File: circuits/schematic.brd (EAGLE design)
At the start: 87.9 x 43.8 mm, 42 parts, among them IC1 MEGA8-P, IC2 MAX481CPA, J1 AVR_SPI_PRG_6PTH

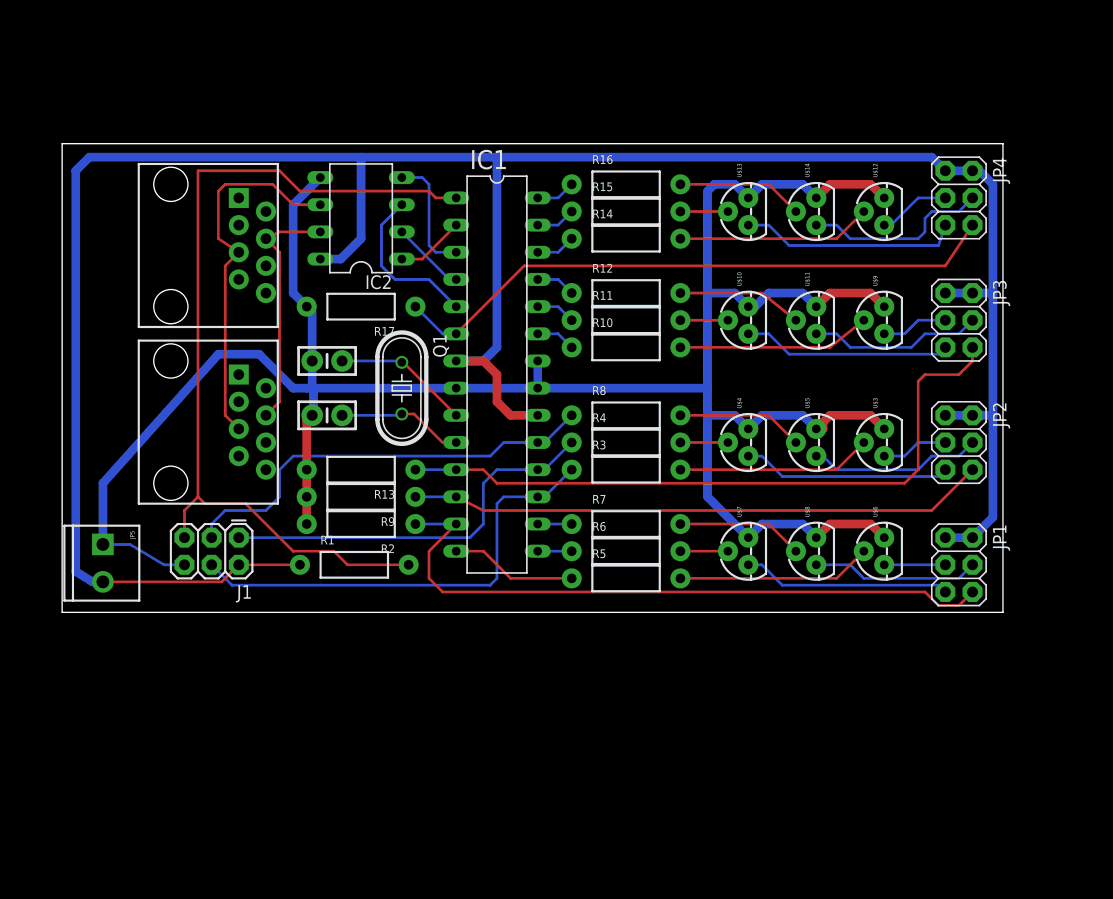
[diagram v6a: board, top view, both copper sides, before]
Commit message: Fix RJ45 jack footprint.
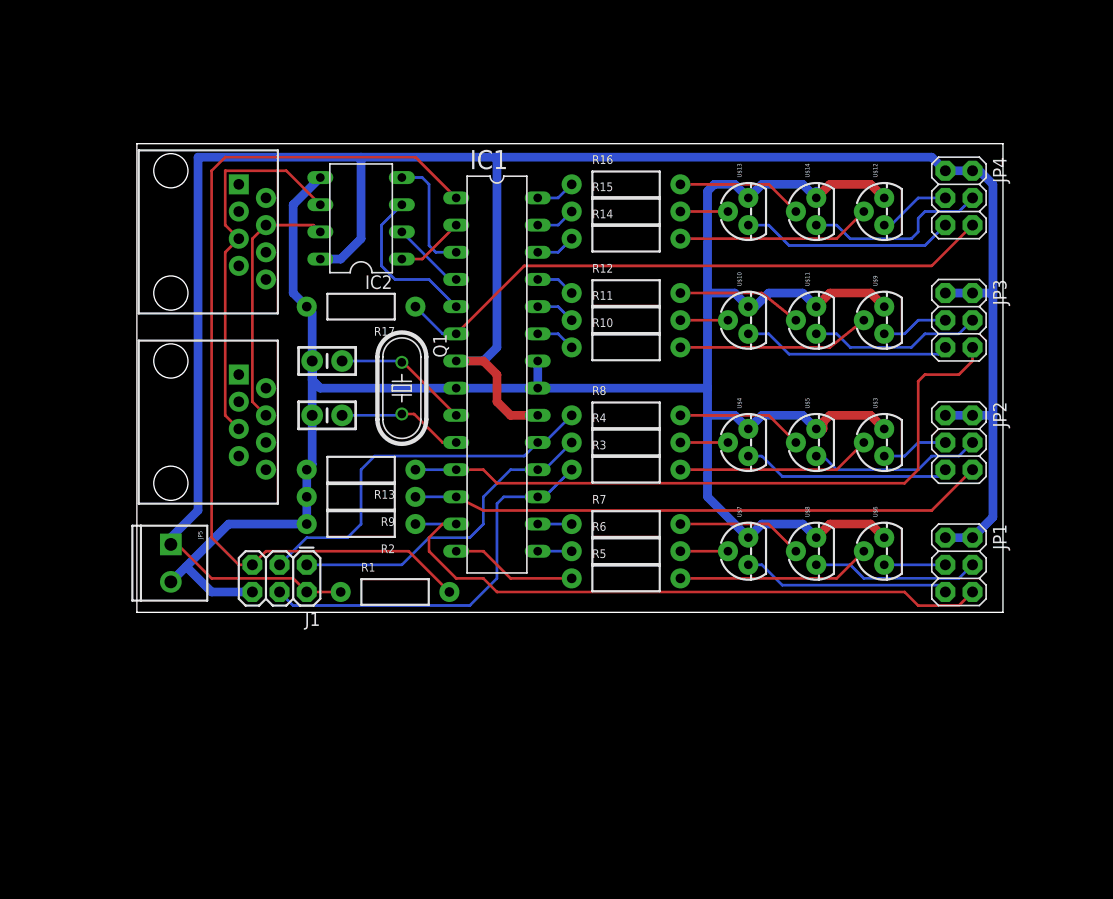
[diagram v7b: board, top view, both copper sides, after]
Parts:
- moved J1 6.84 mm to (26.7, 29.2)
- moved JP5 6.35 mm to (14.0, 31.1)
- moved R1 4.58 mm to (34.9, 26.7)
- moved U$1 1.27 mm to (14.0, 60.3)
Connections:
- net GND: now also JP5.2; no longer JP5.1
- net VCC: now also JP5.1; no longer JP5.2
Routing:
- net VCC: track 239.2 -> 221.1 mm
- net GND: track 221.7 -> 205.5 mm
- net N$55: track 37.0 -> 31.0 mm
- net N$54: track 43.0 -> 37.2 mm
- net N$26: track 40.6 -> 36.1 mm
- net N$18: track 82.3 -> 84.6 mm
- net N$1: track 22.8 -> 24.2 mm
- net N$2: track 34.9 -> 35.9 mm
- net N$14: track 62.3 -> 61.6 mm
- net N$52: track 20.6 -> 20.0 mm
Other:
- board size 87.9 x 43.8 mm -> 81 x 43.8 mm
